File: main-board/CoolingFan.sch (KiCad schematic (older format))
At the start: 0 parts

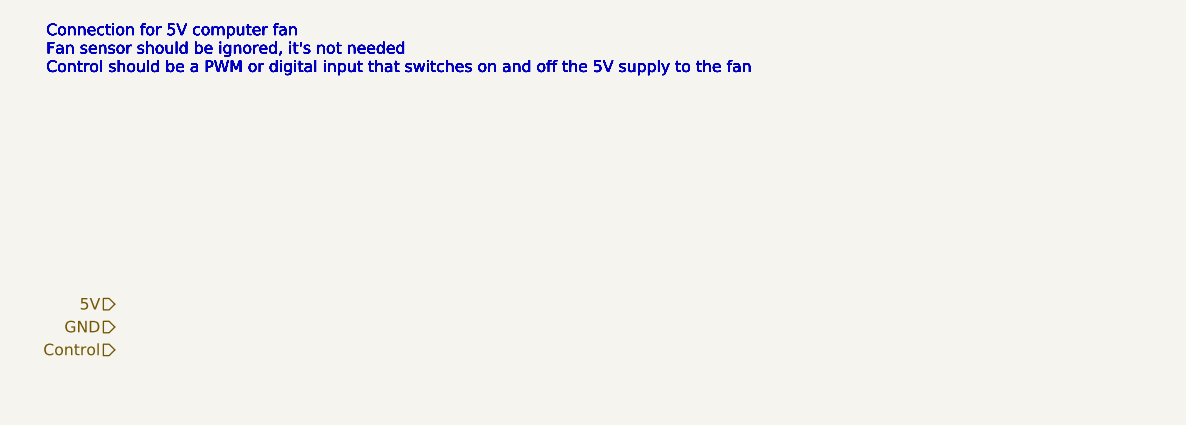
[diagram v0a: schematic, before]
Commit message: Added a few more sheets
Battery
Jetson power button/LED
Over-discharge protection
OpenLog
Power Supply
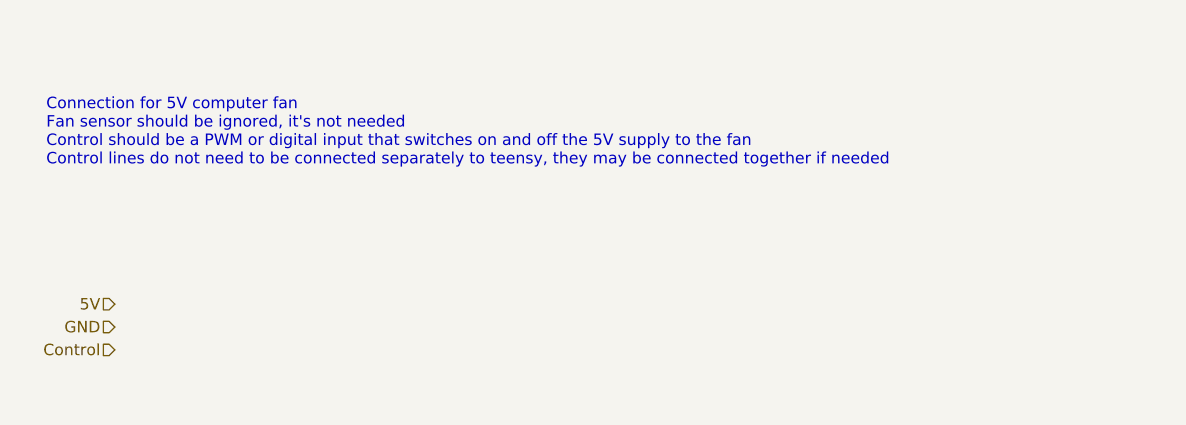
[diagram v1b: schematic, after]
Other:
- note added: "Connection for 5V computer fan\nFan sensor should be ignored, it's not needed\nControl should be a PWM or digital input that switches on and off the 5V supply to the fan\nControl lines do not need to be connected separately to teensy, they may be connected together if needed"
- note removed: "Connection for 5V computer fan\nFan sensor should be ignored, it's not needed\nControl should be a PWM or digital input that switches on and off the 5V supply to the fan"
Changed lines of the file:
@@
 $Descr A4 11693 8268
 encoding utf-8
-Sheet 14 14
+Sheet 14 19
 Title ""
 Date ""
@@
 Text HLabel 5300 2700 0    50   Input ~ 0
 Control
-Text Notes 5000 1500 0    50   ~ 0
-Connection for 5V computer fan\nFan sensor should be ignored, it's not needed\nControl should be a PWM or digital input that switches on and off the 5V supply to the fan
+Text Notes 5000 1900 0    50   ~ 0
+Connection for 5V computer fan\nFan sensor should be ignored, it's not needed\nControl should be a PWM or digital input that switches on and off the 5V supply to the fan\nControl lines do not need to be connected separately to teensy, they may be connected together if needed
 Text HLabel 5300 2600 0    50   Input ~ 0
 GND
-Text Notes 5000 1500 0    50   ~ 0
-Connection for 5V computer fan\nFan sensor should be ignored, it's not needed\nControl should be a PWM or digital input that switches on and off the 5V supply to the fan
-Text Notes 5000 1500 0    50   ~ 0
-Connection for 5V computer fan\nFan sensor should be ignored, it's not needed\nControl should be a PWM or digital input that switches on and off the 5V supply to the fan
-Text Notes 5000 1500 0    50   ~ 0
-Connection for 5V computer fan\nFan sensor should be ignored, it's not needed\nControl should be a PWM or digital input that switches on and off the 5V supply to the fan
 $EndSCHEMATC

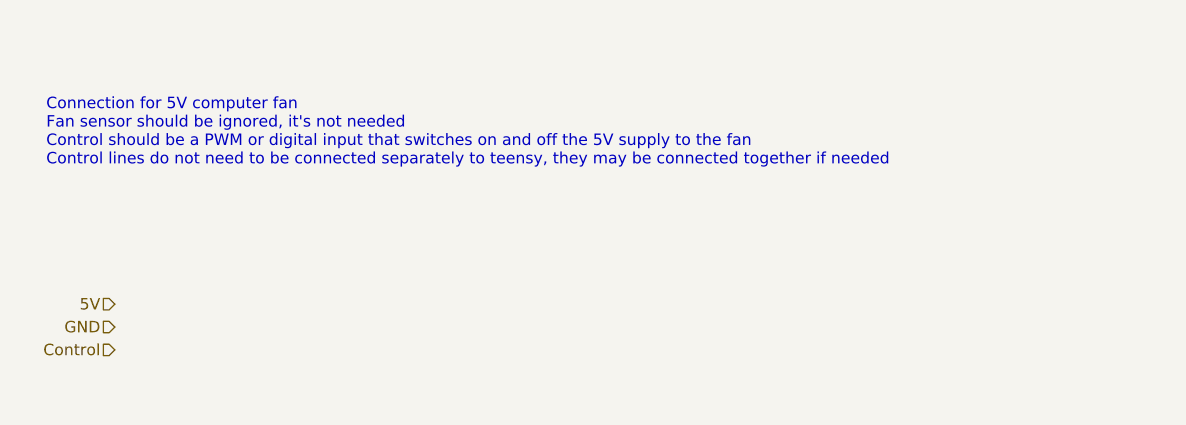
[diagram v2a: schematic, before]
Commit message: Subsheets
Added motor drivers, cooling fans, and openlog
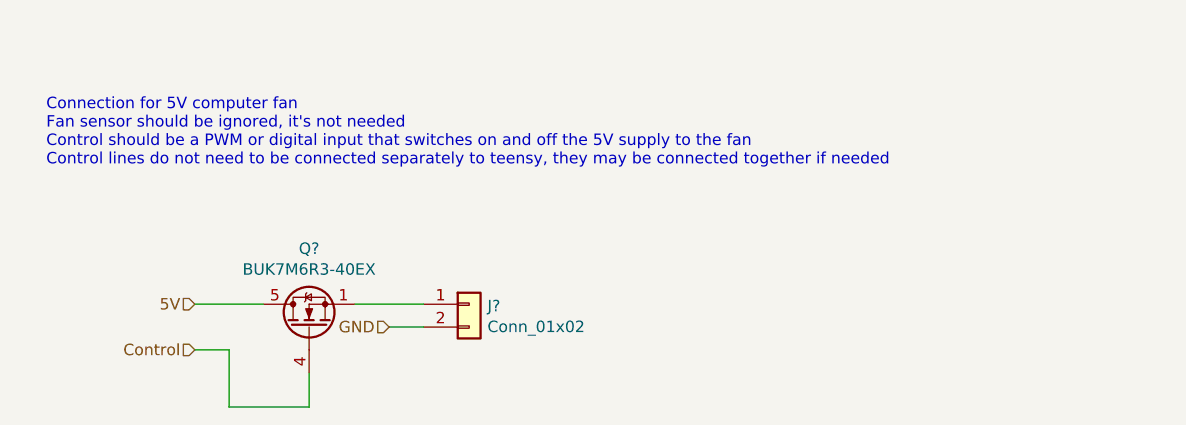
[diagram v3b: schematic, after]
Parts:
- added J?: Conn_01x02, symbol Connector_Generic:Conn_01x02
- added Q?: BUK7M6R3-40EX, Package_TO_SOT_SMD:LFPAK33, symbol Transistor_FET:BUK7M6R3-40EX
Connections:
- net 5V: now also Q?.5 (D)
- net Control: now also Q?.4 (G)
- net GND: now also J?.2 (Pin_2)
- new net: J?.1 (Pin_1), Q?.1 (S), Q?.2 (S), Q?.3 (S)
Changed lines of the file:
@@
 EESchema Schematic File Version 4
+LIBS:main-board-cache
 EELAYER 30 0
 EELAYER END
@@
 Comment4 ""
 $EndDescr
-Text HLabel 5300 2500 0    50   Input ~ 0
+Text HLabel 5650 2500 0    50   Input ~ 0
 5V
-Text HLabel 5300 2700 0    50   Input ~ 0
+Text HLabel 5650 2700 0    50   Input ~ 0
 Control
 Text Notes 5000 1900 0    50   ~ 0
 Connection for 5V computer fan\nFan sensor should be ignored, it's not needed\nControl should be a PWM or digital input that switches on and off the 5V supply to the fan\nControl lines do not need to be connected separately to teensy, they may be connected together if needed
-Text HLabel 5300 2600 0    50   Input ~ 0
+Text HLabel 6500 2600 0    50   Input ~ 0
 GND
+$Comp
+L Transistor_FET:BUK7M6R3-40EX Q?
+U 1 1 60B00463
+P 6150 2600
+AR Path="/60751491/60B00463" Ref="Q?"  Part="1"
+AR Path="/6075154E/60B00463" Ref="Q?"  Part="1"
+AR Path="/6075179F/60B00463" Ref="Q?"  Part="1"
+F 0 "Q?" V 6493 2600 50  0000 C CNN
+F 1 "BUK7M6R3-40EX" V 6402 2600 50  0000 C CNN
+F 2 "Package_TO_SOT_SMD:LFPAK33" H 6350 2525 50  0001 L CIN
+F 3 "https://assets.nexperia.com/documents/data-sheet/BUK7M6R3-40E.pdf" V 6150 2600 50  0001 L CNN
+	1    6150 2600
+	0    -1   -1   0
+$EndComp
+Wire Wire Line
+	5650 2500 5950 2500
+$Comp
+L Connector_Generic:Conn_01x02 J?
+U 1 1 60B1551E
+P 6850 2500
+AR Path="/60751491/60B1551E" Ref="J?"  Part="1"
+AR Path="/6075154E/60B1551E" Ref="J?"  Part="1"
+AR Path="/6075179F/60B1551E" Ref="J?"  Part="1"
+F 0 "J?" H 6930 2492 50  0000 L CNN
+F 1 "Conn_01x02" H 6930 2401 50  0000 L CNN
+F 2 "" H 6850 2500 50  0001 C CNN
+F 3 "~" H 6850 2500 50  0001 C CNN
+	1    6850 2500
+	1    0    0    -1
+$EndComp
+Wire Wire Line
+	6150 2800 6150 2950
+Wire Wire Line
+	6150 2950 5800 2950
+Wire Wire Line
+	5800 2950 5800 2700
+Wire Wire Line
+	5800 2700 5650 2700
+Wire Wire Line
+	6650 2600 6500 2600
+Wire Wire Line
+	6650 2500 6350 2500
 $EndSCHEMATC
